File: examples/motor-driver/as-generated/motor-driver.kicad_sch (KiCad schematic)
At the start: 12 parts, among them J1 VM 2.7-10.8V, J2 MOTOR A, J3 MOTOR B, J4 LOGIC, U1 DRV8833PW

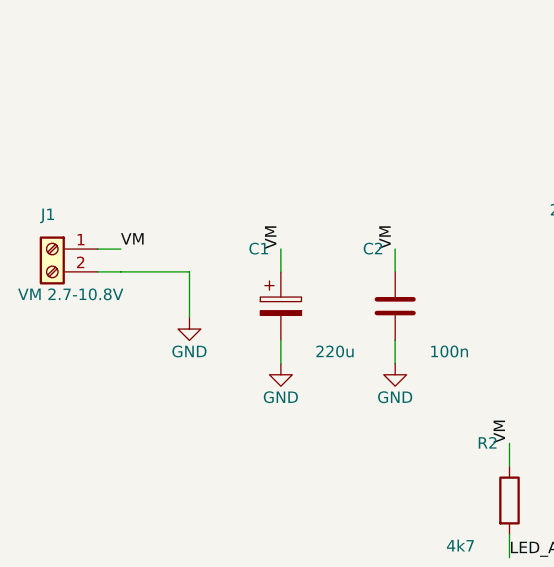
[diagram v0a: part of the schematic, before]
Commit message: Treat the ground plane as part of the drawing
Six reviewer circles, five of them the plane seen from different corners.
The pour now stops 1.2 mm inside the outline so an edge-hugging trace
keeps shell copper outside it; dead-end tongues narrower than 0.9 mm
retract instead of tapering to an acid-trap point in a bent corner; every
piece of the front pour over 8 mm2 holds a stitching via of its own,
placed before the orphan drop so a fenced-off strip gets a via instead of
staying a blank; and zone clearance comes down from 0.4 to 0.25, which is
what lets the plane flow between a 2.54 mm header's pins instead of
slotting the board top to bottom.

The round-twelve tee learns one manner: within two millimetres of the
goal it stands aside, so a rail flows through a bypass capacitor's pad
instead of feeding it by a stub - the carrier's bulk capacitor also moves
onto the VSYS run it was a millimetre south of. And
readability.margin_intrusion now measures symbol fields, power symbols
included: zero findings across KiCad's 18 demo sheets, one real catch on
our own motor sheet, whose power connector - like the FPGA board's -
moves in from the sheet edge so its printed name clears the frame.

Co-Authored-By: Claude Fable 5 <noreply@anthropic.com>
Claude-Session: https://claude.ai/code/session_01DUj7Ltu92tWg159mCSacwY
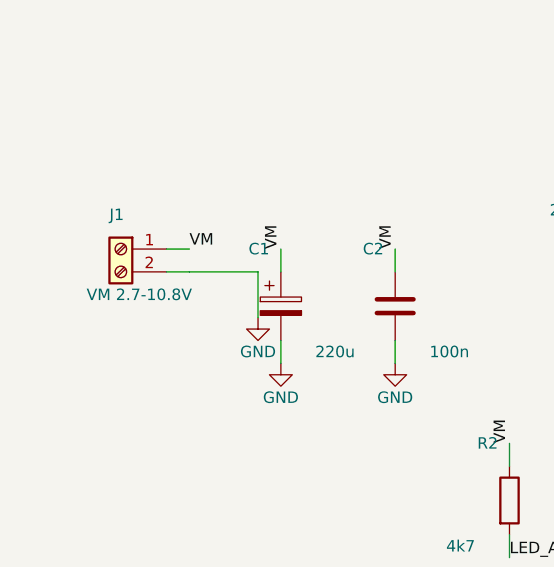
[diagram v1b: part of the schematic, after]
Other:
- moved on the sheet: J1
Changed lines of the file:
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@@
   	(comment 2 "from tools/make_examples.py in sabas0ba/kicad_skills")
   )
-  (wire (pts (xy 35.87 79.82) (xy 38.41 79.82)) (stroke (width 0) (type default)))
-  (label "VM" (at 38.41 79.82 0) (effects (font (size 1.27 1.27)) (justify left bottom)))
-  (wire (pts (xy 35.87 82.36) (xy 38.41 82.36)) (stroke (width 0) (type default)))
-  (symbol (lib_id "Connector:Screw_Terminal_01x02") (at 30.79 79.82 0.0) (mirror y) (unit 1)
-    (exclude_from_sim no) (in_bom yes) (on_board yes) (dnp no)
-    (property "Reference" "J1" (at 29.52 76.01 0) (effects (font (size 1.27 1.27)) (justify right)))
-    (property "Value" "VM 2.7-10.8V" (at 26.98 84.9 0) (effects (font (size 1.27 1.27)) (justify right)))
-    (property "Footprint" "TerminalBlock_Phoenix:TerminalBlock_Phoenix_MKDS-1,5-2_1x02_P5.00mm_Horizontal" (at 30.79 79.82 0) (effects (font (size 1.27 1.27)) hide))
-    (property "Datasheet" "https://www.phoenixcontact.com/product/1729128" (at 30.79 79.82 0) (effects (font (size 1.27 1.27)) hide))
+  (wire (pts (xy 43.49 79.82) (xy 46.03 79.82)) (stroke (width 0) (type default)))
+  (label "VM" (at 46.03 79.82 0) (effects (font (size 1.27 1.27)) (justify left bottom)))
+  (wire (pts (xy 43.49 82.36) (xy 46.03 82.36)) (stroke (width 0) (type default)))
+  (symbol (lib_id "Connector:Screw_Terminal_01x02") (at 38.41 79.82 0.0) (mirror y) (unit 1)
+    (exclude_from_sim no) (in_bom yes) (on_board yes) (dnp no)
+    (property "Reference" "J1" (at 37.14 76.01 0) (effects (font (size 1.27 1.27)) (justify right)))
+    (property "Value" "VM 2.7-10.8V" (at 34.6 84.9 0) (effects (font (size 1.27 1.27)) (justify right)))
+    (property "Footprint" "TerminalBlock_Phoenix:TerminalBlock_Phoenix_MKDS-1,5-2_1x02_P5.00mm_Horizontal" (at 38.41 79.82 0) (effects (font (size 1.27 1.27)) hide))
+    (property "Datasheet" "https://www.phoenixcontact.com/product/1729128" (at 38.41 79.82 0) (effects (font (size 1.27 1.27)) hide))
     (pin "1" (uuid "5a1f741a-09d0-5d38-946e-ffc44a97a438-p1"))
     (pin "2" (uuid "5a1f741a-09d0-5d38-946e-ffc44a97a438-p2"))
@@
     (instances (project "motor-driver" (path "/bddeec65-fa67-5f6a-9af2-d98e98d56e38" (reference "J4") (unit 1))))
   )
-  (wire (pts (xy 38.41 82.36) (xy 46.03 82.36)) (stroke (width 0) (type default)))
-  (wire (pts (xy 46.03 82.36) (xy 46.03 87.44)) (stroke (width 0) (type default)))
+  (wire (pts (xy 46.03 82.36) (xy 53.65 82.36)) (stroke (width 0) (type default)))
+  (wire (pts (xy 53.65 82.36) (xy 53.65 87.44)) (stroke (width 0) (type default)))
   (wire (pts (xy 114.61 74.74) (xy 106.99 74.74)) (stroke (width 0) (type default)))
   (wire (pts (xy 114.61 77.28) (xy 106.99 77.28)) (stroke (width 0) (type default)))
@@
   (wire (pts (xy 188.27 87.44) (xy 188.27 105.22)) (stroke (width 0) (type default)))
   (wire (pts (xy 188.27 105.22) (xy 188.27 110.3)) (stroke (width 0) (type default)))
-  (symbol (lib_id "power:GND") (at 46.03 87.44 0) (unit 1)
+  (symbol (lib_id "power:GND") (at 53.65 87.44 0) (unit 1)
     (exclude_from_sim no) (in_bom no) (on_board yes) (dnp no)
-    (property "Reference" "#PWR01" (at 46.03 87.44 0) (effects (font (size 1.27 1.27)) hide))
-    (property "Value" "GND" (at 46.03 91.25 0) (effects (font (size 1.27 1.27))))
-    (property "Footprint" "" (at 46.03 87.44 0) (effects (font (size 1.27 1.27)) hide))
-    (property "Datasheet" "" (at 46.03 87.44 0) (effects (font (size 1.27 1.27)) hide))
+    (property "Reference" "#PWR01" (at 53.65 87.44 0) (effects (font (size 1.27 1.27)) hide))
+    (property "Value" "GND" (at 53.65 91.25 0) (effects (font (size 1.27 1.27))))
+    (property "Footprint" "" (at 53.65 87.44 0) (effects (font (size 1.27 1.27)) hide))
+    (property "Datasheet" "" (at 53.65 87.44 0) (effects (font (size 1.27 1.27)) hide))
     (pin "1" (uuid "b3b74778-b003-57aa-887f-bb722e1f0c2a-p"))
     (instances (project "motor-driver" (path "/bddeec65-fa67-5f6a-9af2-d98e98d56e38" (reference "#PWR01") (unit 1))))

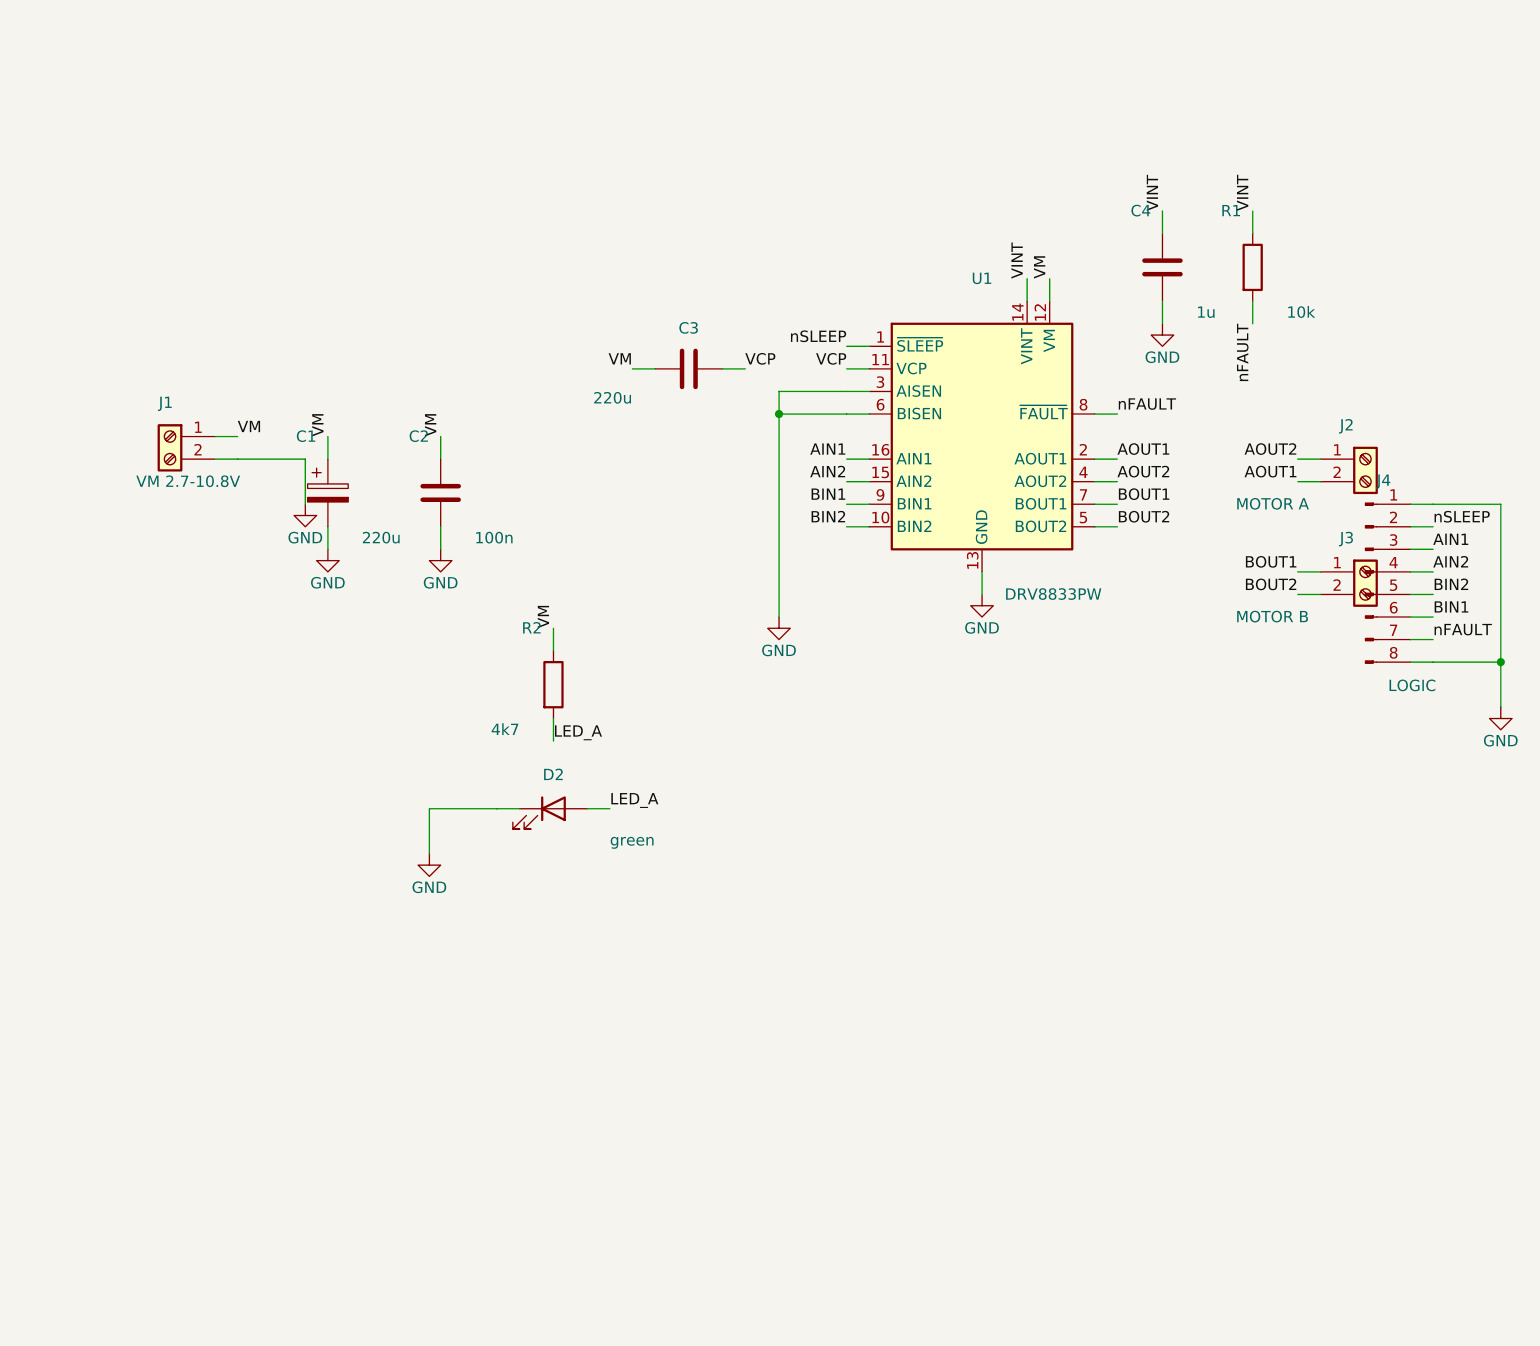
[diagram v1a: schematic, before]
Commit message: Relieve the pads, fillet the joints, and give the board its screw holes
Three of the reviewer's manufacturing points, and they largely fall out
of the one before it - once KiCad fills the plane, the thermal relief it
was already asked for in the file actually appears.

**Thermal relief.** The zones said thermal all along; our own filler
ignored it and flooded every land solid. KiCad's does not, so every
through-hole ground pad now sits in a gap bridged by four spokes and an
iron can bring the joint up without heating a hundred square millimetres
of copper. `layout.solid_pad_connection` reports the setting when a
board turns it off: drilled pads only, because a surface pad reflows in
an oven that is heating the plane anyway and flooding it is often the
better thermal answer.

**Teardrops.** A track entering a land is a step change in width, and a
step change is where copper tears - the connector gets levered on and
off, the drill wanders, and the crack starts at the corner. `_teardrops`
replaces the first stretch of each run with a three-step taper into the
land, checked against its neighbours before it is kept, so a fillet
never eats the clearance a fine-pitch escape needs. It *replaces* rather
than overlays: laying the taper on top of the run drew the same copper
twice, and `route.acute_angle` reported all thirty of them, correctly.
`route.mixed_track_widths` learns what a fillet looks like so a properly
filleted board does not read as one nobody decided the width of.

**Mounting holes.** Four M3 holes near the corners, placed before the
router runs because they are obstacles, and slid along the edges or a
little inboard where a connector body has the corner - the motor board
and the op-amp take three, which is what those floorplans have room for.
Grounded on the motor driver, whose chassis is metal and part of the
shield, plain on the rest: bonding the enclosure to the reference is the
enclosure's decision, not the board's.

Two things that fell out of placing par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
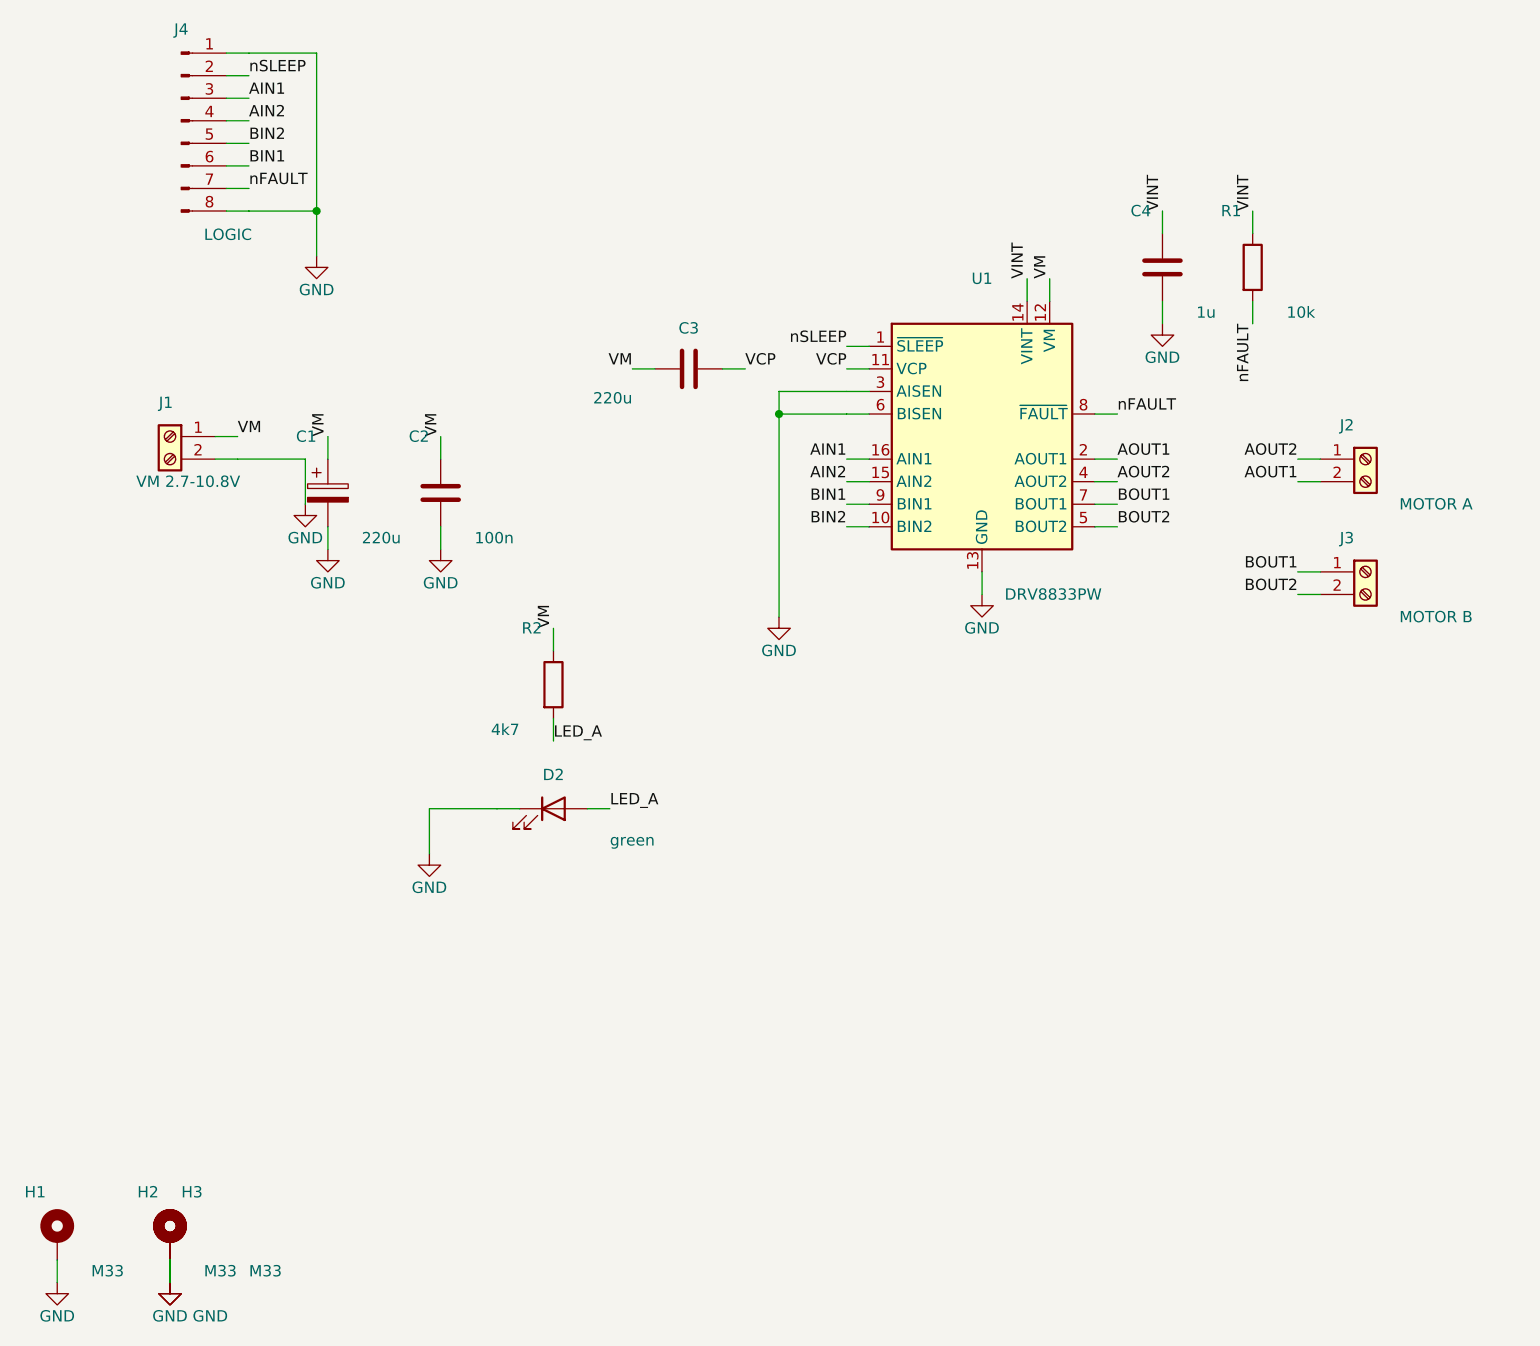
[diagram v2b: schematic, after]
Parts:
- added H1, H2, H3: M33, MountingHole:MountingHole_3.2mm_M3_Pad, symbol Mechanical:MountingHole_Pad
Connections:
- net GND: now also H1.1, H2.1, H3.1
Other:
- moved on the sheet: J4
